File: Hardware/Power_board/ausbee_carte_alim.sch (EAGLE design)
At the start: 21 parts

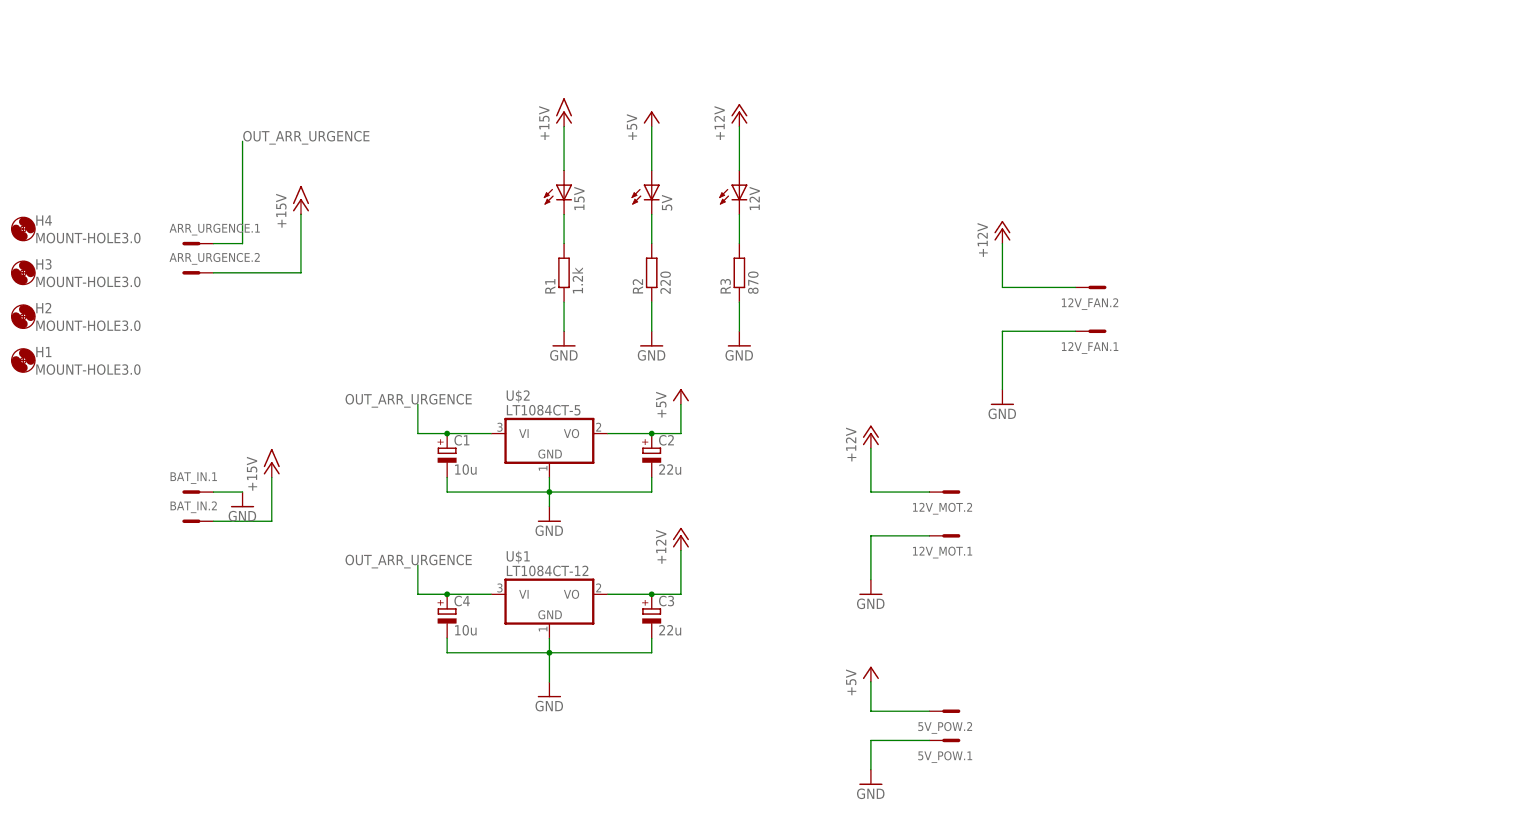
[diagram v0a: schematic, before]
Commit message: modification on power board: add relay and fuse
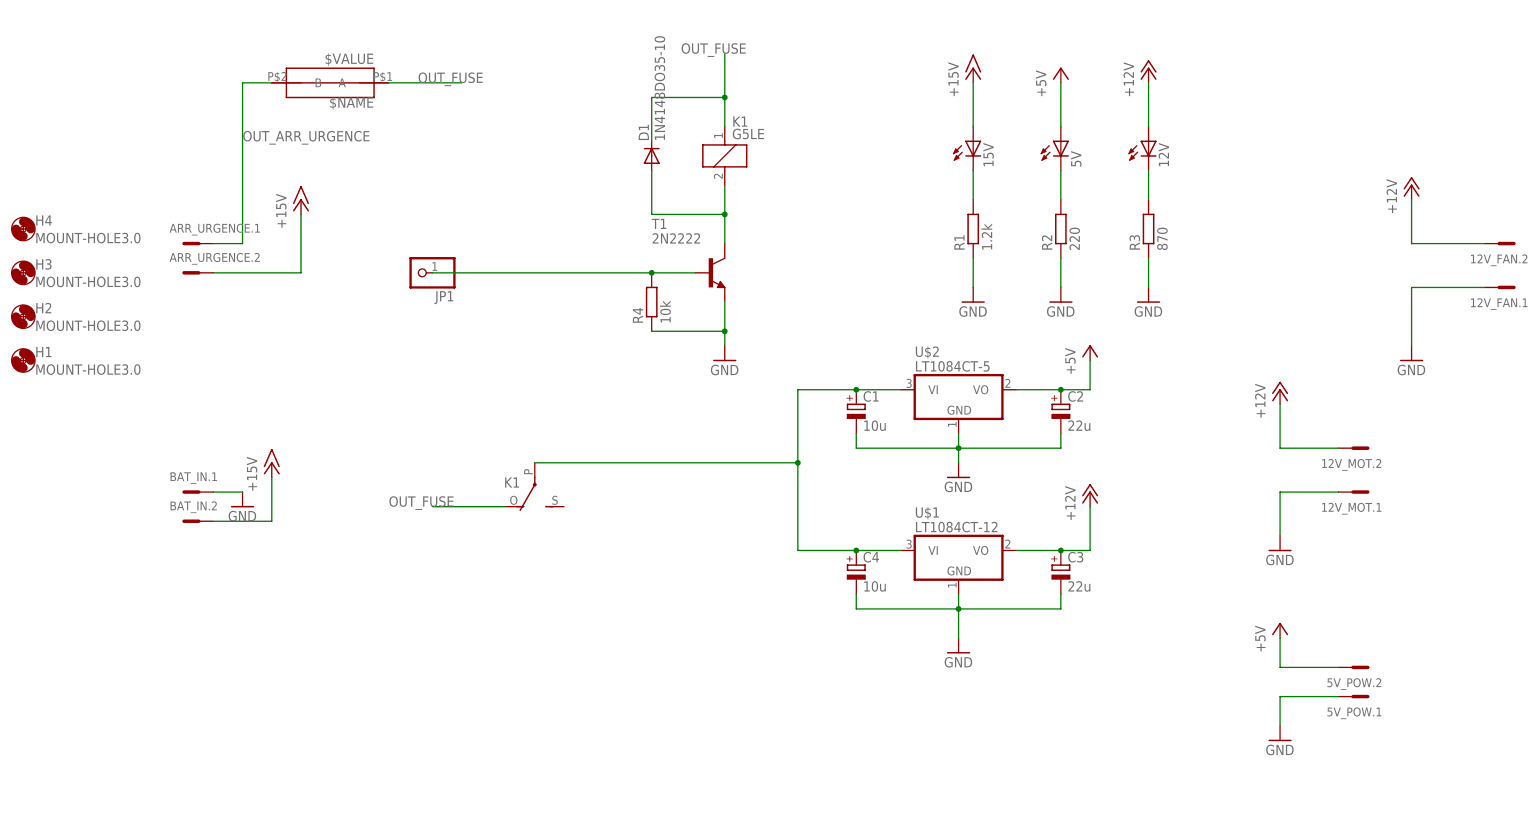
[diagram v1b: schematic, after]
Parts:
- added D1: 1N4148DO35-10, diode:1N4148DO35-10
- added JP1: (no value), pinhead:PINHD-1X1
- added K1: G5LE, relay:G5LE
- added R4: 10k, rcl:R-EU_0309/V
- added T1: 2N2222, transistor:2N2222
- added U$3: FUSE_CAR, eirbot:FUSE_CAR
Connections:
- new net N$4: C1.+, C4.+, K12.P, U$1.VI, U$2.VI
- new net N$5: D1.A, K11.2, T1.C
- new net N$6: JP1.1, R4.2, T1.B
- new net OUT_FUSE: D1.C, K11.1, K12.O, U$3.A
- net GND: now also R4.1, T1.E
- net OUT_ARR_URGENCE: now also U$3.B; no longer C1.+, C4.+, U$1.VI, U$2.VI
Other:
- moved on the sheet: 12V, 12V_FAN.1, 12V_FAN.2, 12V_MOT.1, 12V_MOT.2, 15V, 5V, 5V_POW.1, 5V_POW.2, C1, C2, C3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

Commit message: add MOS instead of bipolar and change fuse footprint
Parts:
- removed U$3: FUSE_CAR, eirbot:FUSE_CAR
- added F1: FUSESHK20L, fuse:FUSESHK20L
- T1: value 2N2222 -> (none); device transistor:2N2222 -> zetex:NMOSSOT23
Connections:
- net GND: now also T1.S; no longer T1.E
- net N$5: now also T1.D; no longer T1.C
- net N$6: now also T1.G; no longer T1.B
- net OUT_ARR_URGENCE: now also F1.1; no longer U$3.B
- net OUT_FUSE: now also F1.2; no longer U$3.A
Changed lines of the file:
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@@
 <part name="H4" library="holes" deviceset="MOUNT-HOLE" device="3.0"/>
 <part name="K1" library="relay" deviceset="G5LE" device=""/>
-<part name="T1" library="transistor" deviceset="2N2222" device=""/>
 <part name="GND10" library="supply1" deviceset="GND" device=""/>
 <part name="R4" library="rcl" deviceset="R-EU_" device="0309/V" value="10k"/>
 <part name="JP1" library="pinhead" deviceset="PINHD-1X1" device=""/>
-<part name="U$3" library="eirbot" deviceset="FUSE_CAR" device=""/>
 <part name="D1" library="diode" deviceset="1N4148" device="DO35-10"/>
+<part name="T1" library="zetex" deviceset="NMOSSOT23" device=""/>
+<part name="F1" library="fuse" deviceset="FUSE" device="SHK20L"/>
 </parts>
 <sheets>
@@
 <instance part="K1" gate="1" x="99.06" y="96.52"/>
 <instance part="K1" gate="2" x="66.04" y="40.64" rot="R180"/>
-<instance part="T1" gate="G$1" x="96.52" y="76.2"/>
 <instance part="GND10" gate="1" x="99.06" y="60.96"/>
 <instance part="R4" gate="G$1" x="86.36" y="71.12" rot="R90"/>
 <instance part="JP1" gate="G$1" x="45.72" y="76.2" rot="R180"/>
-<instance part="U$3" gate="G$1" x="30.48" y="109.22" rot="R180"/>
 <instance part="D1" gate="G$1" x="86.36" y="96.52" rot="R90"/>
+<instance part="T1" gate="A" x="99.06" y="78.74"/>
+<instance part="F1" gate="G$1" x="30.48" y="109.22"/>
 </instances>
 <busses>
@@
 <segment>
 <pinref part="GND10" gate="1" pin="GND"/>
-<pinref part="T1" gate="G$1" pin="E"/>
 <wire x1="99.06" y1="63.5" x2="99.06" y2="66.04" width="0.1524" layer="91"/>
 <pinref part="R4" gate="G$1" pin="1"/>
-<wire x1="99.06" y1="66.04" x2="99.06" y2="71.12" width="0.1524" layer="91"/>
 <wire x1="86.36" y1="66.04" x2="99.06" y2="66.04" width="0.1524" layer="91"/>
+<pinref part="T1" gate="A" pin="S"/>
+<wire x1="99.06" y1="66.04" x2="99.06" y2="73.66" width="0.1524" layer="91"/>
 <junction x="99.06" y="66.04"/>
 </segment>
@@
 <wire x1="15.24" y1="81.28" x2="15.24" y2="109.22" width="0.1524" layer="91"/>
 <label x="15.24" y="99.06" size="1.778" layer="95"/>
-<pinref part="U$3" gate="G$1" pin="B"/>
-<wire x1="20.32" y1="109.22" x2="15.24" y2="109.22" width="0.1524" layer="91"/>
+<pinref part="F1" gate="G$1" pin="1"/>
+<wire x1="15.24" y1="109.22" x2="25.4" y2="109.22" width="0.1524" layer="91"/>
 </segment>
 </net>
@@
 <net name="N$5" class="0">
 <segment>
-<pinref part="T1" gate="G$1" pin="C"/>
 <pinref part="K1" gate="1" pin="2"/>
-<wire x1="99.06" y1="81.28" x2="99.06" y2="86.36" width="0.1524" layer="91"/>
+<wire x1="99.06" y1="83.82" x2="99.06" y2="86.36" width="0.1524" layer="91"/>
 <pinref part="D1" gate="G$1" pin="A"/>
 <wire x1="99.06" y1="86.36" x2="99.06" y2="91.44" width="0.1524" layer="91"/>
@@
 <wire x1="86.36" y1="86.36" x2="99.06" y2="86.36" width="0.1524" layer="91"/>
 <junction x="99.06" y="86.36"/>
+<pinref part="T1" gate="A" pin="D"/>
 </segment>
 </net>
@@
 <segment>
 <pinref part="R4" gate="G$1" pin="2"/>
-<pinref part="T1" gate="G$1" pin="B"/>
-<wire x1="86.36" y1="76.2" x2="93.98" y2="76.2" width="0.1524" layer="91"/>
 <pinref part="JP1" gate="G$1" pin="1"/>
 <wire x1="86.36" y1="76.2" x2="48.26" y2="76.2" width="0.1524" layer="91"/>
+<pinref part="T1" gate="A" pin="G"/>
+<wire x1="86.36" y1="76.2" x2="93.98" y2="76.2" width="0.1524" layer="91"/>
 <junction x="86.36" y="76.2"/>
 </segment>
@@
 <net name="OUT_FUSE" class="0">
 <segment>
-<pinref part="U$3" gate="G$1" pin="A"/>
-<wire x1="40.64" y1="109.22" x2="53.34" y2="109.22" width="0.1524" layer="91"/>
+<wire x1="35.56" y1="109.22" x2="53.34" y2="109.22" width="0.1524" layer="91"/>
 <label x="45.72" y="109.22" size="1.778" layer="95"/>
-</segment>
-<segment>
+<pinref part="F1" gate="G$1" pin="2"/>
+</segment>
+<segment>

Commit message: Power board V2, adaptator GPIO
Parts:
- C2, C3: device rcl:CPOL-EUE5-8.5 -> rcl:CPOL-EUCT7343
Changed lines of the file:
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@@
 <grid distance="0.1" unitdist="inch" unit="inch" style="lines" multiple="1" display="no" altdistance="0.01" altunitdist="inch" altunit="inch"/>
 <layers>
-<layer number="1" name="Top" color="4" fill="1" visible="no" active="no"/>
-<layer number="2" name="Route2" color="1" fill="3" visible="no" active="no"/>
-<layer number="3" name="Route3" color="4" fill="3" visible="no" active="no"/>
-<layer number="4" name="Route4" color="1" fill="4" visible="no" active="no"/>
-<layer number="5" name="Route5" color="4" fill="4" visible="no" active="no"/>
-<layer number="6" name="Route6" color="1" fill="8" visible="no" active="no"/>
-<layer number="7" name="Route7" color="4" fill="8" visible="no" active="no"/>
-<layer number="8" name="Route8" color="1" fill="2" visible="no" active="no"/>
-<layer number="9" name="Route9" color="4" fill="2" visible="no" active="no"/>
-<layer number="10" name="Route10" color="1" fill="7" visible="no" active="no"/>
-<layer number="11" name="Route11" color="4" fill="7" visible="no" active="no"/>
-<layer number="12" name="Route12" color="1" fill="5" visible="no" active="no"/>
-<layer number="13" name="Route13" color="4" fill="5" visible="no" active="no"/>
-<layer number="14" name="Route14" color="1" fill="6" visible="no" active="no"/>
-<layer number="15" name="Route15" color="4" fill="6" visible="no" active="no"/>
-<layer number="16" name="Bottom" color="1" fill="1" visible="no" active="no"/>
-<layer number="17" name="Pads" color="2" fill="1" visible="no" active="no"/>
-<layer number="18" name="Vias" color="2" fill="1" visible="no" active="no"/>
-<layer number="19" name="Unrouted" color="6" fill="1" visible="no" active="no"/>
-<layer number="20" name="Dimension" color="15" fill="1" visible="no" active="no"/>
-<layer number="21" name="tPlace" color="7" fill="1" visible="no" active="no"/>
-<layer number="22" name="bPlace" color="7" fill="1" visible="no" active="no"/>
-<layer number="23" name="tOrigins" color="15" fill="1" visible="no" active="no"/>
-<layer number="24" name="bOrigins" color="15" fill="1" visible="no" active="no"/>
-<layer number="25" name="tNames" color="7" fill="1" visible="no" active="no"/>
-<layer number="26" name="bNames" color="7" fill="1" visible="no" active="no"/>
-<layer number="27" name="tValues" color="7" fill="1" visible="no" active="no"/>
-<layer number="28" name="bValues" color="7" fill="1" visible="no" active="no"/>
+<layer number="1" name="Top" color="4" fill="1" visible="yes" active="no"/>
+<layer number="2" name="Route2" color="1" fill="3" visible="yes" active="no"/>
+<layer number="3" name="Route3" color="4" fill="3" visible="yes" active="no"/>
+<layer number="4" name="Route4" color="1" fill="4" visible="yes" active="no"/>
+<layer number="5" name="Route5" color="4" fill="4" visible="yes" active="no"/>
+<layer number="6" name="Route6" color="1" fill="8" visible="yes" active="no"/>
+<layer number="7" name="Route7" color="4" fill="8" visible="yes" active="no"/>
+<layer number="8" name="Route8" color="1" fill="2" visible="yes" active="no"/>
+<layer number="9" name="Route9" color="4" fill="2" visible="yes" active="no"/>
+<layer number="10" name="Route10" color="1" fill="7" visible="yes" active="no"/>
+<layer number="11" name="Route11" color="4" fill="7" visible="yes" active="no"/>
+<layer number="12" name="Route12" color="1" fill="5" visible="yes" active="no"/>
+<layer number="13" name="Route13" color="4" fill="5" visible="yes" active="no"/>
+<layer number="14" name="Route14" color="1" fill="6" visible="yes" active="no"/>
+<layer number="15" name="Route15" color="4" fill="6" visible="yes" active="no"/>
+<layer number="16" name="Bottom" color="1" fill="1" visible="yes" active="no"/>
+<layer number="17" name="Pads" color="2" fill="1" visible="yes" active="no"/>
+<layer number="18" name="Vias" color="2" fill="1" visible="yes" active="no"/>
+<layer number="19" name="Unrouted" color="6" fill="1" visible="yes" active="no"/>
+<layer number="20" name="Dimension" color="15" fill="1" visible="yes" active="no"/>
+<layer number="21" name="tPlace" color="7" fill="1" visible="yes" active="no"/>
+<layer number="22" name="bPlace" color="7" fill="1" visible="yes" active="no"/>
+<layer number="23" name="tOrigins" color="15" fill="1" visible="yes" active="no"/>
+<layer number="24" name="bOrigins" color="15" fill="1" visible="yes" active="no"/>
+<layer number="25" name="tNames" color="7" fill="1" visible="yes" active="no"/>
+<layer number="26" name="bNames" color="7" fill="1" visible="yes" active="no"/>
+<layer number="27" name="tValues" color="7" fill="1" visible="yes" active="no"/>
+<layer number="28" name="bValues" color="7" fill="1" visible="yes" active="no"/>
 <layer number="29" name="tStop" color="7" fill="3" visible="no" active="no"/>
 <layer number="30" name="bStop" color="7" fill="6" visible="no" active="no"/>
@@
 <layer number="35" name="tGlue" color="7" fill="4" visible="no" active="no"/>
 <layer number="36" name="bGlue" color="7" fill="5" visible="no" active="no"/>
-<layer number="37" name="tTest" color="7" fill="1" visible="no" active="no"/>
-<layer number="38" name="bTest" color="7" fill="1" visible="no" active="no"/>
+<layer number="37" name="tTest" color="7" fill="1" visible="yes" active="no"/>
+<layer number="38" name="bTest" color="7" fill="1" visible="yes" active="no"/>
 <layer number="39" name="tKeepout" color="4" fill="11" visible="no" active="no"/>
 <layer number="40" name="bKeepout" color="1" fill="11" visible="no" active="no"/>
@@
 <layer number="44" name="Drills" color="7" fill="1" visible="no" active="no"/>
 <layer number="45" name="Holes" color="7" fill="1" visible="no" active="no"/>
-<layer number="46" name="Milling" color="3" fill="1" visible="no" active="no"/>
-<layer number="47" name="Measures" color="7" fill="1" visible="no" active="no"/>
-<layer number="48" name="Document" color="7" fill="1" visible="no" active="no"/>
-<layer number="49" name="Reference" color="7" fill="1" visible="no" active="no"/>
-<layer number="51" name="tDocu" color="7" fill="1" visible="no" active="no"/>
-<layer number="52" name="bDocu" color="7" fill="1" visible="no" active="no"/>
+<layer number="46" name="Milling" color="3" fill="1" visible="yes" active="no"/>
+<layer number="47" name="Measures" color="7" fill="1" visible="yes" active="no"/>
+<layer number="48" name="Document" color="7" fill="1" visible="yes" active="no"/>
+<layer number="49" name="Reference" color="7" fill="1" visible="yes" active="no"/>
+<layer number="51" name="tDocu" color="7" fill="1" visible="yes" active="no"/>
+<layer number="52" name="bDocu" color="7" fill="1" visible="yes" active="no"/>
 <layer number="91" name="Nets" color="2" fill="1" visible="yes" active="yes"/>
 <layer number="92" name="Busses" color="1" fill="1" visible="yes" active="yes"/>
@@
 <part name="P+5" library="supply1" deviceset="+5V" device=""/>
 <part name="C1" library="rcl" deviceset="CPOL-EU" device="E5-8.5" value="10u"/>
-<part name="C2" library="rcl" deviceset="CPOL-EU" device="E5-8.5" value="22u"/>
-<part name="C3" library="rcl" deviceset="CPOL-EU" device="E5-8.5" value="22u"/>
+<part name="C2" library="rcl" deviceset="CPOL-EU" device="CT7343" value="22u"/>
+<part name="C3" library="rcl" deviceset="CPOL-EU" device="CT7343" value="22u"/>
 <part name="C4" library="rcl" deviceset="CPOL-EU" device="E5-8.5" value="10u"/>
 <part name="ARR_URGENCE" library="con-phoenix-381_l" deviceset="MCV2" device=""/>
